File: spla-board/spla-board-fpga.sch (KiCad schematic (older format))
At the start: 36 parts, among them J2 J_JTAG, U1 LFE5U-45F-BG256

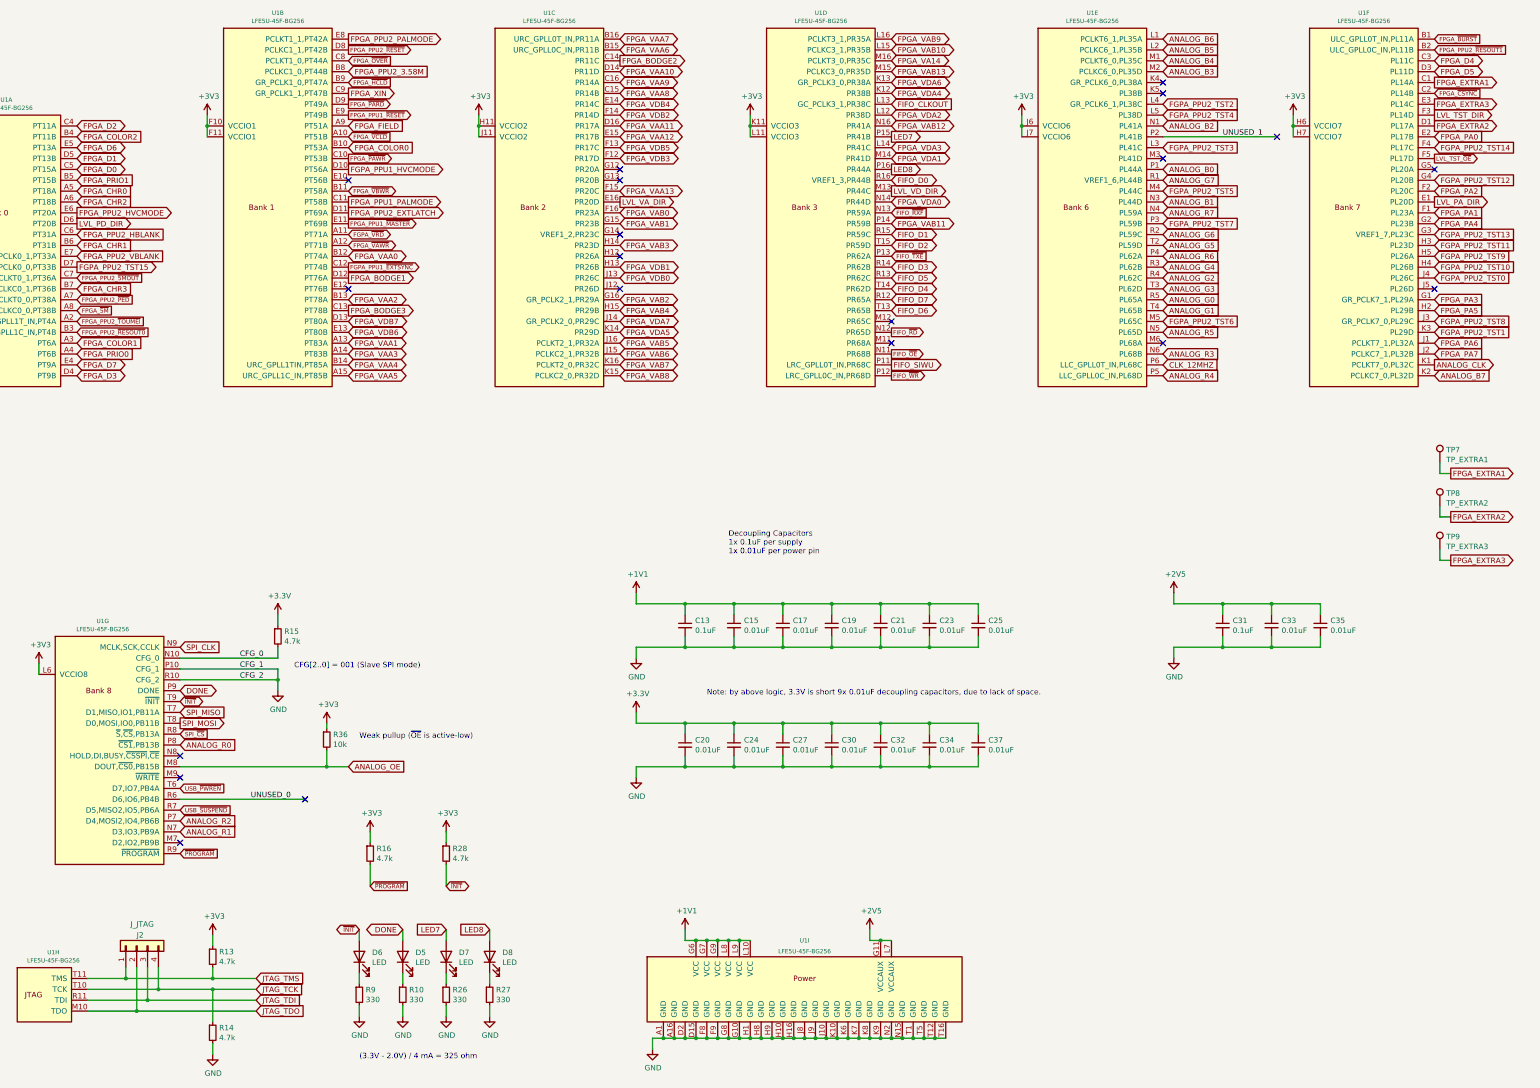
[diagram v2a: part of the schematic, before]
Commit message: schematic/pcb: Pinswap entire FPGA to put LEDs/TPs on south edge.
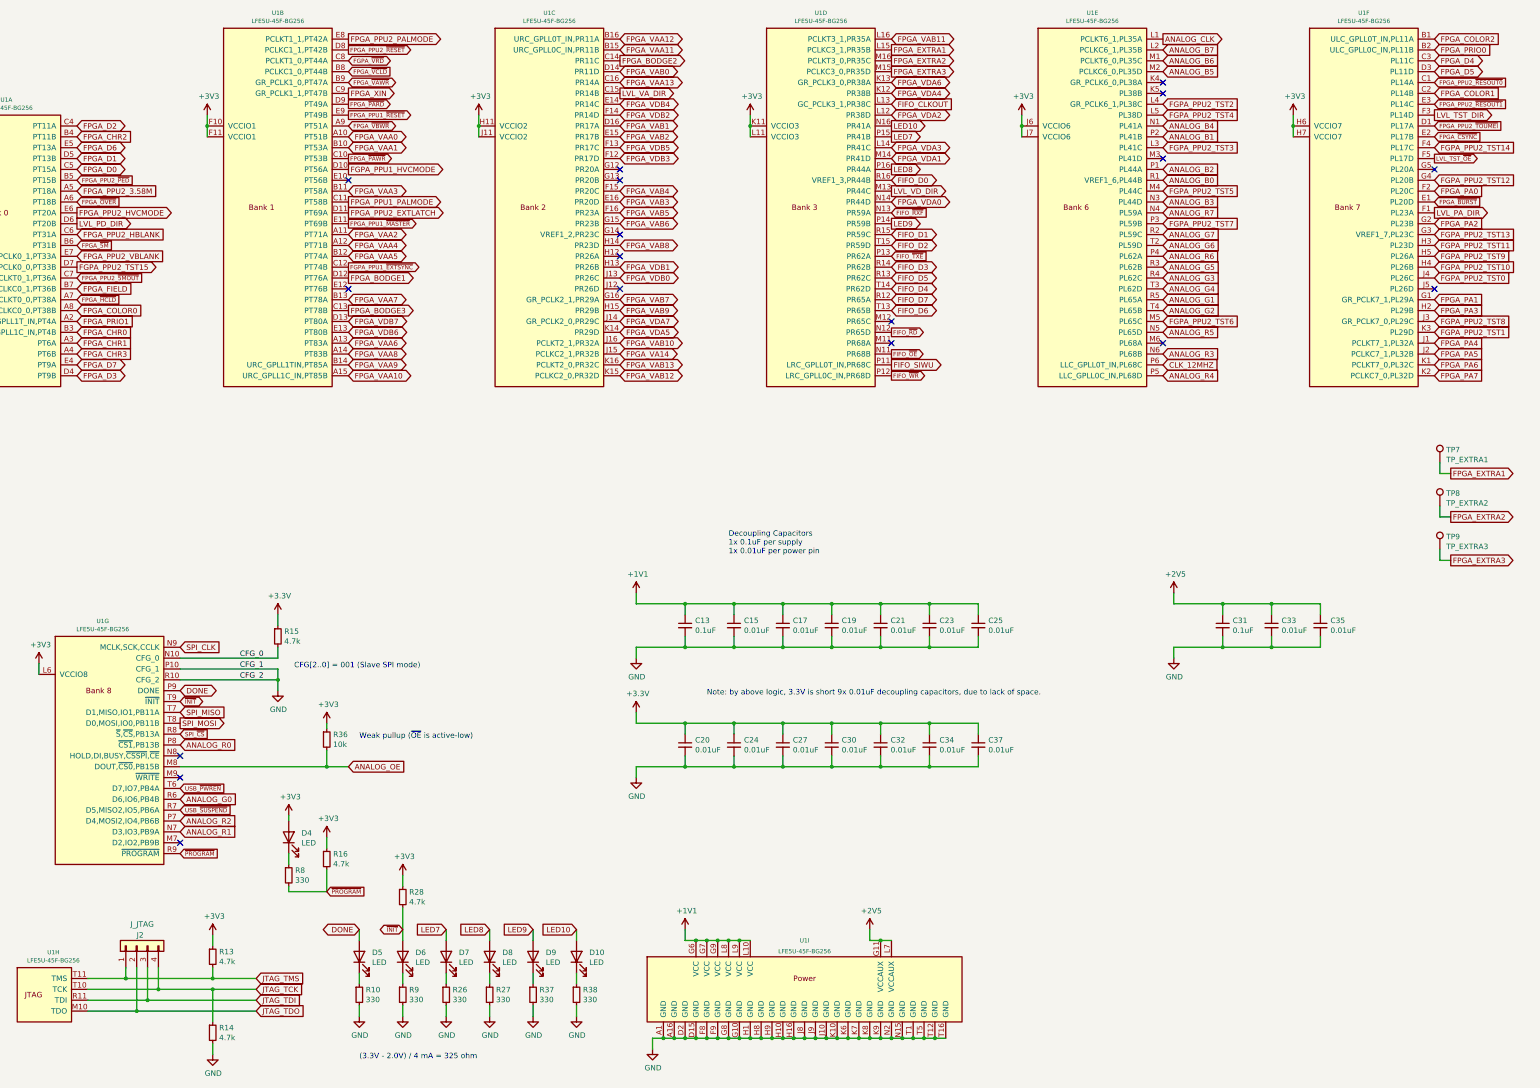
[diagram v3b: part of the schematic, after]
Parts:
- added D10, D4, D9: LED, LED_SMD:LED_0805_2012Metric, symbol Device:LED
- added R37, R38, R8: 330, Resistor_SMD:R_0603_1608Metric, symbol Device:R_Small
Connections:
- net UNUSED_0 is gone; now on net ANALOG_G0: U1.R6 (D6,IO6,PB4B)
- net UNUSED_1 is gone; now on net ANALOG_B1: U1.P2 (PL41B)
- net +3V3: now also D4.2 (A)
- net ANALOG_B0: now also U1.R1 (VREF1_6,PL44B); no longer U1.P1 (PL44A)
- net ANALOG_B1: no longer U1.N3 (PL44D)
- net ANALOG_B2: now also U1.P1 (PL44A); no longer U1.N1 (PL41A)
- net ANALOG_B3: now also U1.N3 (PL44D); no longer U1.M2 (PCLKC6_0,PL35D)
- net ANALOG_B4: now also U1.N1 (PL41A); no longer U1.M1 (PCLKT6_0,PL35C)
- net ANALOG_B5: now also U1.M2 (PCLKC6_0,PL35D); no longer U1.L2 (PCLKC6_1,PL35B)
- net ANALOG_B6: now also U1.M1 (PCLKT6_0,PL35C); no longer U1.L1 (PCLKT6_1,PL35A)
- net ANALOG_B7: now also U1.L2 (PCLKC6_1,PL35B); no longer U1.K2 (PCLKC7_0,PL32D)
- net ANALOG_CLK: now also U1.L1 (PCLKT6_1,PL35A); no longer U1.K1 (PCLKT7_0,PL32C)
- net ANALOG_G0: no longer U1.R5 (PL65A)
- net ANALOG_G1: now also U1.R5 (PL65A); no longer U1.T4 (PL65B)
- net ANALOG_G2: now also U1.T4 (PL65B); no longer U1.R4 (PL62C)
- net ANALOG_G3: now also U1.R4 (PL62C); no longer U1.T3 (PL62D)
- net ANALOG_G4: now also U1.T3 (PL62D); no longer U1.R3 (PL62B)
- net ANALOG_G5: now also U1.R3 (PL62B); no longer U1.T2 (PL59D)
- net ANALOG_G6: now also U1.T2 (PL59D); no longer U1.R2 (PL59C)
- net ANALOG_G7: now also U1.R2 (PL59C); no longer U1.R1 (VREF1_6,PL44B)
- net FGPA_~VRD~: now also U1.C8 (PCLKT1_0,PT44A); no longer U1.A11 (PT71A)
- net FPGA_CHR0: now also U1.B3 (ULC_GPLL1C_IN,PT4B); no longer U1.A5 (PT18A)
- net FPGA_CHR1: now also U1.A3 (PT6A); no longer U1.B6 (PT31B)
- net FPGA_CHR2: now also U1.B4 (PT11B); no longer U1.A6 (PT18B)
- net FPGA_CHR3: now also U1.A4 (PT6B); no longer U1.B7 (PCLKC0_1,PT36B)
- net FPGA_COLOR0: now also U1.A8 (PCLKC0_0,PT38B); no longer U1.B10 (PT53A)
- net FPGA_COLOR1: now also U1.C2 (PL14B); no longer U1.A3 (PT6A)
- net FPGA_COLOR2: now also U1.B1 (ULC_GPLL0T_IN,PL11A); no longer U1.B4 (PT11B)
- net FPGA_EXTRA1: now also U1.L15 (PCLKC3_1,PR35B); no longer U1.C1 (PL14A)
- net FPGA_EXTRA2: now also U1.M16 (PCLKT3_0,PR35C); no longer U1.D1 (PL17A)
- net FPGA_EXTRA3: now also U1.M15 (PCLKC3_0,PR35D); no longer U1.E3 (PL14C)
- net FPGA_FIELD: now also U1.B7 (PCLKC0_1,PT36B); no longer U1.A9 (PT51A)
- net FPGA_PA0: now also U1.F2 (PL20C); no longer U1.E2 (PL17B)
- net FPGA_PA1: now also U1.G1 (GR_PCLK7_1,PL29A); no longer U1.F1 (PL23A)
- net FPGA_PA2: now also U1.G2 (PL23B); no longer U1.F2 (PL20C)
- net FPGA_PA3: now also U1.H2 (PL29B); no longer U1.G1 (GR_PCLK7_1,PL29A)
- net FPGA_PA4: now also U1.J1 (PCLKT7_1,PL32A); no longer U1.G2 (PL23B)
- net FPGA_PA5: now also U1.J2 (PCLKC7_1,PL32B); no longer U1.H2 (PL29B)
- net FPGA_PA6: now also U1.K1 (PCLKT7_0,PL32C); no longer U1.J1 (PCLKT7_1,PL32A)
- net FPGA_PA7: now also U1.K2 (PCLKC7_0,PL32D); no longer U1.J2 (PCLKC7_1,PL32B)
- net FPGA_PPU2_3.58M: now also U1.A5 (PT18A); no longer U1.B8 (PCLKC1_0,PT44B)
- net FPGA_PPU2_~PED~: now also U1.B5 (PT15B); no longer U1.A7 (PCLKT0_0,PT38A)
- net FPGA_PPU2_~RESOUT0~: now also U1.C1 (PL14A); no longer U1.B3 (ULC_GPLL1C_IN,PT4B)
- net FPGA_PPU2_~RESOUT1~: now also U1.E3 (PL14C); no longer U1.B2 (ULC_GPLL0C_IN,PL11B)
- net FPGA_PPU2_~TOUMEI~: now also U1.D1 (PL17A); no longer U1.A2 (ULC_GPLL1T_IN,PT4A)
- net FPGA_PRIO0: now also U1.B2 (ULC_GPLL0C_IN,PL11B); no longer U1.A4 (PT6B)
- net FPGA_PRIO1: now also U1.A2 (ULC_GPLL1T_IN,PT4A); no longer U1.B5 (PT15B)
- net FPGA_VA14: now also U1.J15 (PCLKC2_1,PR32B); no longer U1.M16 (PCLKT3_0,PR35C)
- net FPGA_VAA0: now also U1.A10 (PT51B); no longer U1.B12 (PT74A)
- net FPGA_VAA1: now also U1.B10 (PT53A); no longer U1.A13 (PT83A)
- net FPGA_VAA10: now also U1.A15 (URC_GPLL1C_IN,PT85B); no longer U1.D14 (PR11D)
- net FPGA_VAA11: now also U1.B15 (URC_GPLL0C_IN,PR11B); no longer U1.D16 (PR17A)
- net FPGA_VAA12: now also U1.B16 (URC_GPLL0T_IN,PR11A); no longer U1.E15 (PR17B)
- net FPGA_VAA13: now also U1.C16 (PR14A); no longer U1.F15 (PR20C)
- net FPGA_VAA2: now also U1.A11 (PT71A); no longer U1.B13 (PT78A)
- net FPGA_VAA3: now also U1.B11 (PT58A); no longer U1.A14 (PT83B)
- net FPGA_VAA4: now also U1.A12 (PT71B); no longer U1.B14 (URC_GPLL1TIN,PT85A)
- net FPGA_VAA5: now also U1.B12 (PT74A); no longer U1.A15 (URC_GPLL1C_IN,PT85B)
- net FPGA_VAA6: now also U1.A13 (PT83A); no longer U1.B15 (URC_GPLL0C_IN,PR11B)
- net FPGA_VAA7: now also U1.B13 (PT78A); no longer U1.B16 (URC_GPLL0T_IN,PR11A)
- net FPGA_VAA8: now also U1.A14 (PT83B); no longer U1.C15 (PR14B)
- net FPGA_VAA9: now also U1.B14 (URC_GPLL1TIN,PT85A); no longer U1.C16 (PR14A)
- net FPGA_VAB0: now also U1.D14 (PR11D); no longer U1.F16 (PR23A)
- net FPGA_VAB1: now also U1.D16 (PR17A); no longer U1.G15 (PR23B)
- net FPGA_VAB10: now also U1.J16 (PCLKT2_1,PR32A); no longer U1.L15 (PCLKC3_1,PR35B)
- net FPGA_VAB11: now also U1.L16 (PCLKT3_1,PR35A); no longer U1.P14 (PR59B)
- net FPGA_VAB12: now also U1.K15 (PCLKC2_0,PR32D); no longer U1.N16 (PR41A)
- net FPGA_VAB13: now also U1.K16 (PCLKT2_0,PR32C); no longer U1.M15 (PCLKC3_0,PR35D)
- net FPGA_VAB2: now also U1.E15 (PR17B); no longer U1.G16 (GR_PCLK2_1,PR29A)
- net FPGA_VAB3: now also U1.E16 (PR20D); no longer U1.H14 (PR23D)
- net FPGA_VAB4: now also U1.F15 (PR20C); no longer U1.H15 (PR29B)
- net FPGA_VAB5: now also U1.F16 (PR23A); no longer U1.J16 (PCLKT2_1,PR32A)
- net FPGA_VAB6: now also U1.G15 (PR23B); no longer U1.J15 (PCLKC2_1,PR32B)
- net FPGA_VAB7: now also U1.G16 (GR_PCLK2_1,PR29A); no longer U1.K16 (PCLKT2_0,PR32C)
- net FPGA_VAB8: now also U1.H14 (PR23D); no longer U1.K15 (PCLKC2_0,PR32D)
- net FPGA_VAB9: now also U1.H15 (PR29B); no longer U1.L16 (PCLKT3_1,PR35A)
- net FPGA_~5M~: now also U1.B6 (PT31B); no longer U1.A8 (PCLKC0_0,PT38B)
- net FPGA_~BURST~: now also U1.E1 (PL20D); no longer U1.B1 (ULC_GPLL0T_IN,PL11A)
- net FPGA_~CSYNC~: now also U1.E2 (PL17B); no longer U1.C2 (PL14B)
- net FPGA_~HCLD: now also U1.A7 (PCLKT0_0,PT38A); no longer U1.B9 (GR_PCLK1_0,PT47A)
- net FPGA_~OVER~: now also U1.A6 (PT18B); no longer U1.C8 (PCLKT1_0,PT44A)
- net FPGA_~VAWR~: now also U1.B9 (GR_PCLK1_0,PT47A); no longer U1.A12 (PT71B)
- net FPGA_~VBWR~: now also U1.A9 (PT51A); no longer U1.B11 (PT58A)
- net FPGA_~VCLD~: now also U1.B8 (PCLKC1_0,PT44B); no longer U1.A10 (PT51B)
- net GND: now also R37.2, R38.2
- net LVL_PA_DIR: now also U1.F1 (PL23A); no longer U1.E1 (PL20D)
- net LVL_VA_DIR: now also U1.C15 (PR14B); no longer U1.E16 (PR20D)
- net ~PROGRAM: now also R8.2
- new net: D9.1 (K), R37.1
- new net: D10.1 (K), R38.1
- new net: D4.1 (K), R8.1
- new net LED10: D10.2 (A), U1.N16 (PR41A)
- new net LED9: D9.2 (A), U1.P14 (PR59B)
- no-connect marks 20 -> 18
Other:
- moved on the sheet: D5, D6, R10, R16, R28, R9

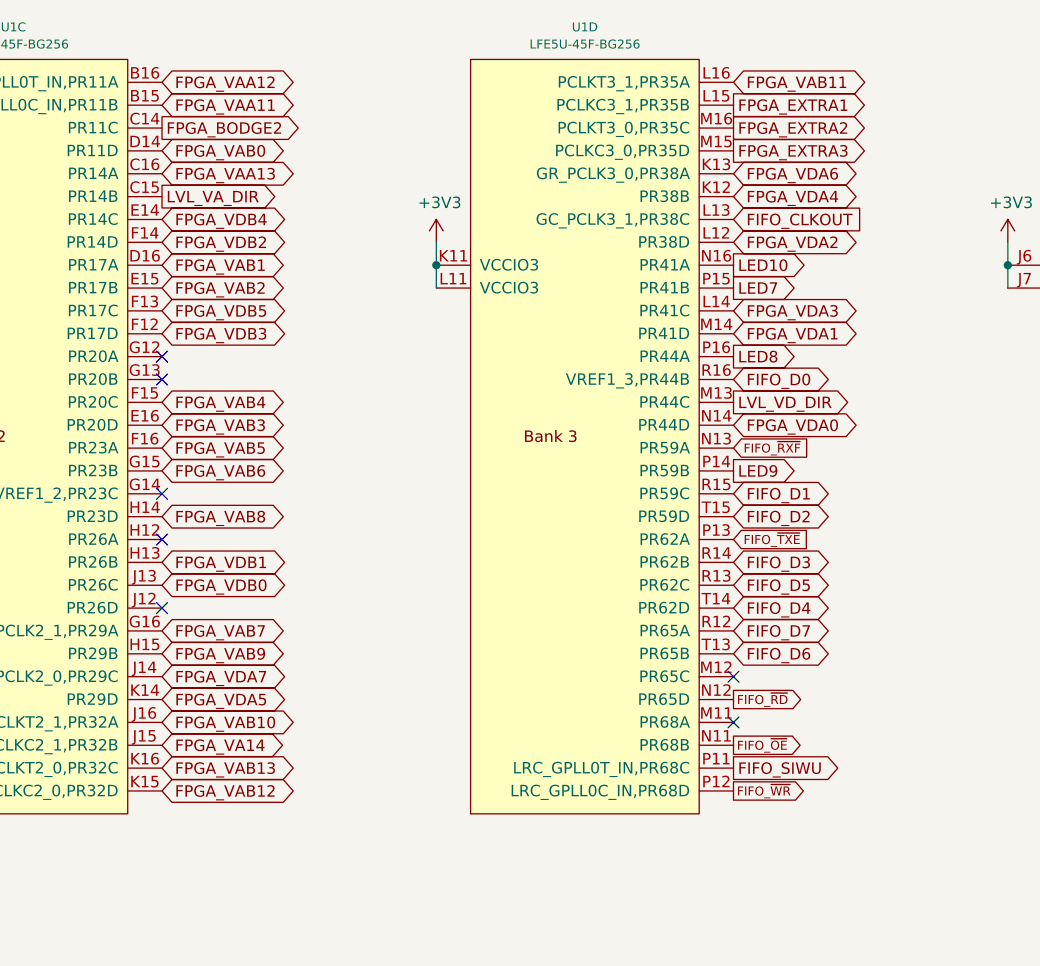
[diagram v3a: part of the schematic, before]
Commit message: pcb/schematic: Rework layout for 0.65mm PPU footprint, as well as other minor issues.
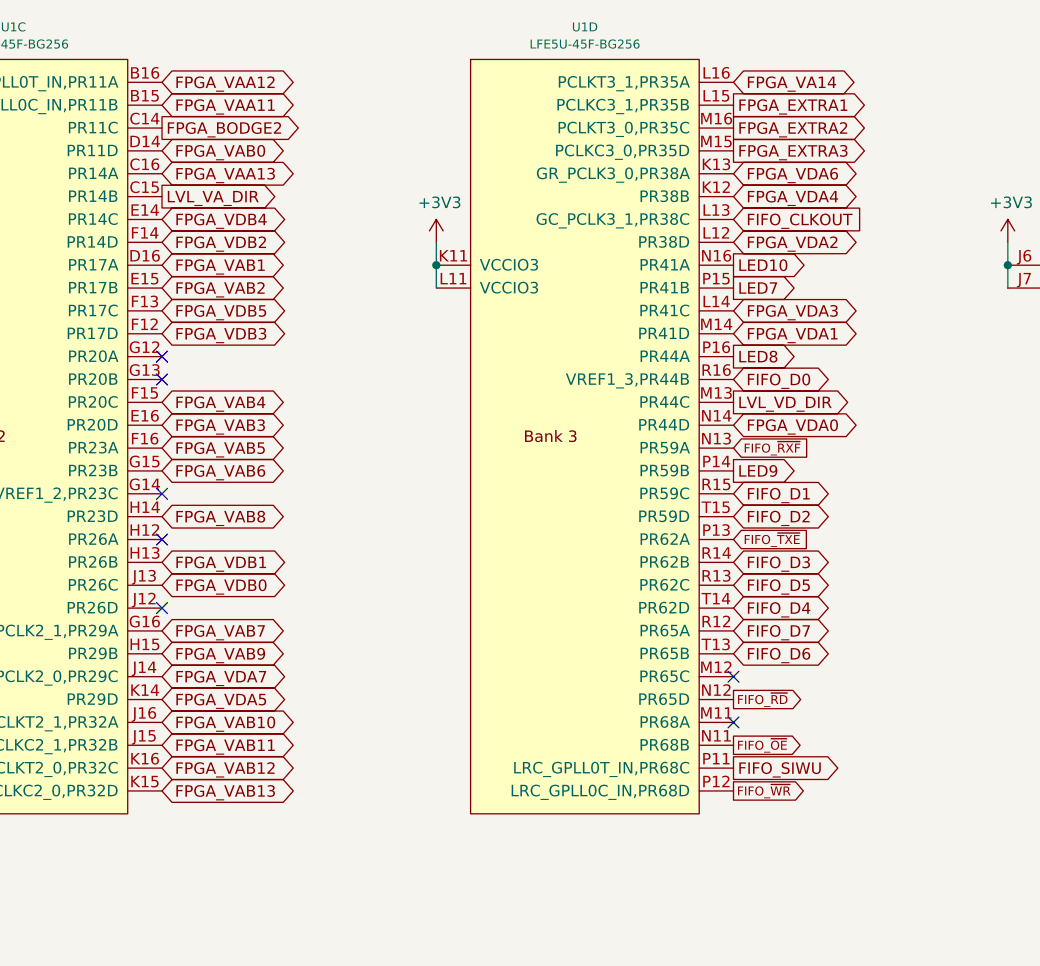
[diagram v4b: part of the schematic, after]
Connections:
- net FPGA_VA14: now also U1.L16 (PCLKT3_1,PR35A); no longer U1.J15 (PCLKC2_1,PR32B)
- net FPGA_VAB11: now also U1.J15 (PCLKC2_1,PR32B); no longer U1.L16 (PCLKT3_1,PR35A)
- net FPGA_VAB12: now also U1.K16 (PCLKT2_0,PR32C); no longer U1.K15 (PCLKC2_0,PR32D)
- net FPGA_VAB13: now also U1.K15 (PCLKC2_0,PR32D); no longer U1.K16 (PCLKT2_0,PR32C)
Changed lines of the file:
@@
 Text GLabel 7150 1700 2    50   BiDi ~ 0
 FPGA_VAA13
-Text GLabel 7150 4200 2    50   BiDi ~ 0
+Text GLabel 9650 1300 2    50   BiDi ~ 0
 FPGA_VA14
 Text GLabel 7150 3200 2    50   BiDi ~ 0
@@
 Text GLabel 7150 4100 2    50   BiDi ~ 0
 FPGA_VAB10
-Text GLabel 9650 1300 2    50   BiDi ~ 0
+Text GLabel 7150 4200 2    50   BiDi ~ 0
 FPGA_VAB11
+Text GLabel 7150 4300 2    50   BiDi ~ 0
+FPGA_VAB12
 Text GLabel 7150 4400 2    50   BiDi ~ 0
-FPGA_VAB12
-Text GLabel 7150 4300 2    50   BiDi ~ 0
 FPGA_VAB13
 Text GLabel 4650 1500 2    39   BiDi ~ 0
